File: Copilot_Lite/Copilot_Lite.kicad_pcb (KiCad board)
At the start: 4 copper layers, 65 x 56 mm, 80 parts, among them J1 POWER_MODES, J11 SERIAL_MODE, J12 SERIAL_VOLTAGE_SELECT, J2 JACK_POWER_IN, J3 USB_POWER_IN, J4 USB_PC, J6 5V_ENABLE, J7 SERIAL_AND_GPIO, J8 JACK_POWER_OUT, J9 USB_POWER_OUT, Q1 BSS138, Q2 BUK7M27-80EX, Q3 BUK7M27-80EX, Q4 BSS138, Q5 BSS138, Q6 BSS138, Q7 BSS138, Q8 BSS138, Q9 BSS138, U1 LM74502, U2 LM74502, U3 AP2204K-ADJ, U4 AP2204K-ADJ, U5 FT230XS, U6 SN74LV1T125, U7 SN74LV1T125, U8 SN74LV1T125, U9 SN74LV1T125

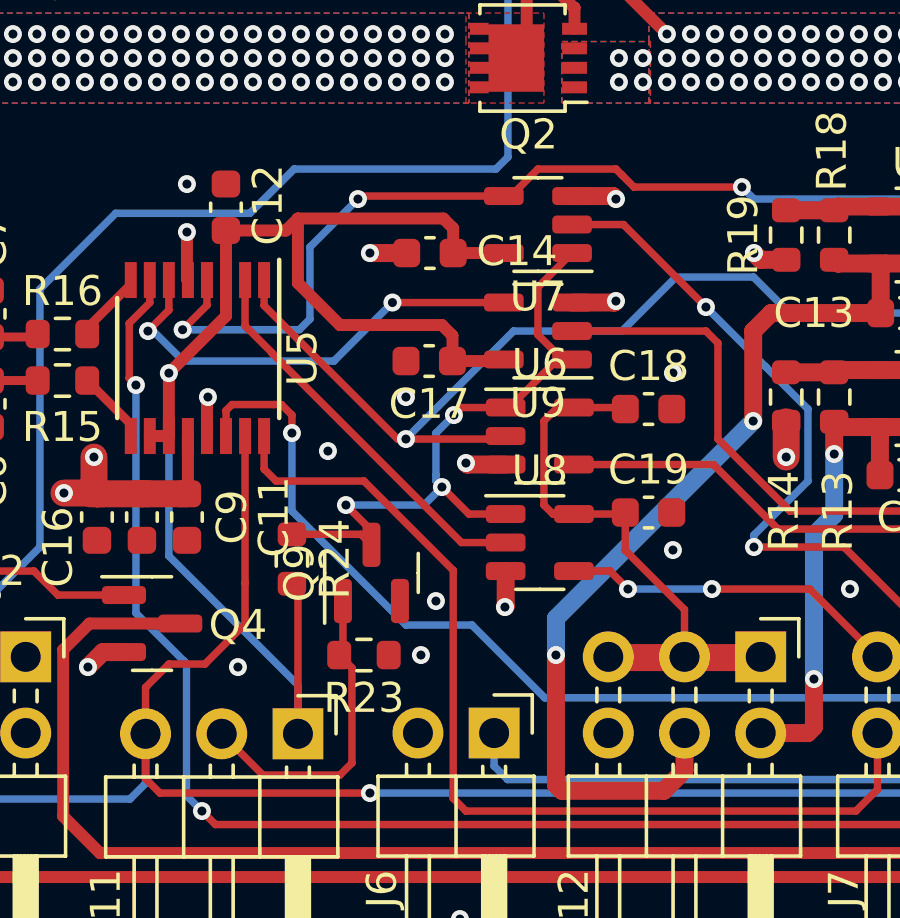
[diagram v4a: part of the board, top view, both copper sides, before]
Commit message: lite: Cleaned PCB silkscreen and fixed all warnings.
Signed-off-by: Adrien Ricciardi <aricciardi@baylibre.com>
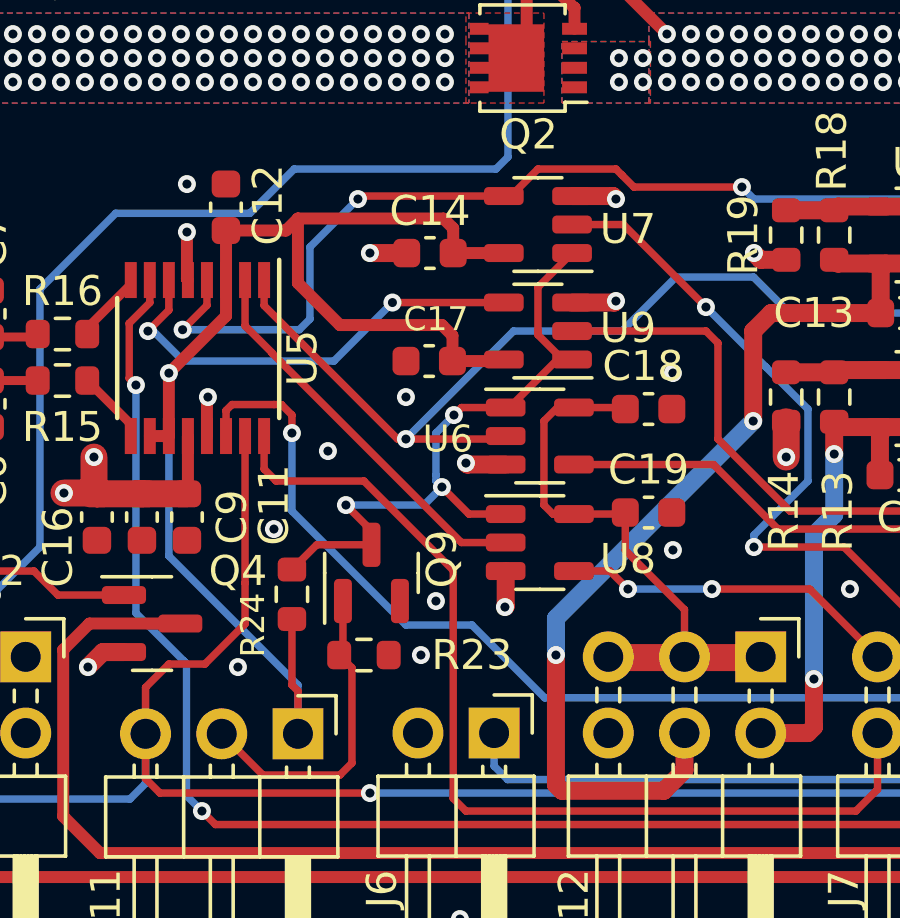
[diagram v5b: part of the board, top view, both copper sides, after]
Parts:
- moved R24 1.17 mm to (89.4, 101.4)
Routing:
- net +3.3VA: track 48.2 -> 47.0 mm
- net GND: vias 59 -> 60
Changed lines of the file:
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@@
     (property "Sheetname" "Controller")
     (attr smd)
-    (fp_text reference "U9" (at 0 -2.4) (layer "F.SilkS")
+    (fp_text reference "U9" (at -3 0.1) (layer "F.SilkS")
         (effects (font (size 1 1) (thickness 0.15)))
     )
@@
     (property "Sheetname" "Controller")
     (attr smd)
-    (fp_text reference "U7" (at 0 -2.4) (layer "F.SilkS")
+    (fp_text reference "U7" (at -3 -0.15) (layer "F.SilkS")
         (effects (font (size 1 1) (thickness 0.15)))
     )
@@
     (property "Sheetname" "Controller")
     (attr smd)
-    (fp_text reference "U6" (at 0 -2.4) (layer "F.SilkS")
-        (effects (font (size 1 1) (thickness 0.15)))
+    (fp_text reference "U6" (at -3.0625 0.1) (layer "F.SilkS")
+        (effects (font (size 0.9 0.9) (thickness 0.15)))
     )
     (fp_text value "SN74LV1T125" (at 0 2.4) (layer "F.Fab") hide
@@
     (property "ki_keywords" "cap capacitor")
     (attr smd)
-    (fp_text reference "C18" (at 0 -1.43) (layer "F.SilkS")
+    (fp_text reference "C18" (at -0.1875 -1.43) (layer "F.SilkS")
         (effects (font (size 1 1) (thickness 0.15)))
     )
@@
     (property "ki_keywords" "cap capacitor")
     (attr smd)
-    (fp_text reference "C14" (at -2.9 0.06) (layer "F.SilkS")
+    (fp_text reference "C14" (at 0 1.4) (layer "F.SilkS")
         (effects (font (size 1 1) (thickness 0.15)))
     )
@@
     (property "ki_keywords" "R res resistor")
     (attr smd)
-    (fp_text reference "R23" (at 0 -1.43) (layer "F.SilkS")
+    (fp_text reference "R23" (at -3.6 0) (layer "F.SilkS")
         (effects (font (size 1 1) (thickness 0.15)))
     )
@@
     (property "ki_keywords" "N-Channel MOSFET")
     (attr smd)
-    (fp_text reference "Q4" (at 2.8625 0.05) (layer "F.SilkS")
+    (fp_text reference "Q4" (at 2.8625 -1.75) (layer "F.SilkS")
         (effects (font (size 1 1) (thickness 0.15)))
     )
@@
     (property "ki_keywords" "N-Channel MOSFET")
     (attr smd)
-    (fp_text reference "Q9" (at 0 -2.4 90) (layer "F.SilkS")
+    (fp_text reference "Q9" (at 0.4625 2.35 90) (layer "F.SilkS")
         (effects (font (size 1 1) (thickness 0.15)))
     )
@@
     (property "Sheetname" "Controller")
     (attr smd)
-    (fp_text reference "U8" (at 0 -2.4) (layer "F.SilkS")
+    (fp_text reference "U8" (at 2.9375 0.55) (layer "F.SilkS")
         (effects (font (size 1 1) (thickness 0.15)))
     )
@@
   )
   (footprint "Resistor_SMD:R_0603_1608Metric" (layer "F.Cu")
-    (at 89.4 100.2 -90)
+    (at 89.4 101.375 -90)
     (descr "Resistor SMD 0603 (1608 Metric), square (rectangular) end terminal, IPC_7351 nominal, (Body size source: IPC-SM-782 page 72, https://www.pcb-3d.com/wordpress/wp-content/uploads/ipc-sm-782a_amendment_1_and_2.pdf), generated with kicad-footprint-generator")
     (tags "resistor")
@@
     (property "ki_keywords" "R res resistor")
     (attr smd)
-    (fp_text reference "R24" (at 0 -1.43 90) (layer "F.SilkS")
-        (effects (font (size 1 1) (thickness 0.15)))
+    (fp_text reference "R24" (at 1.025 1.3 90) (layer "F.SilkS")
+        (effects (font (size 0.8 0.8) (thickness 0.15)))
     )
     (fp_text value "10K" (at 0 1.43 90) (layer "F.Fab") hide
@@
     (property "ki_keywords" "cap capacitor")
     (attr smd)
-    (fp_text reference "C11" (at 0 -2.9 90) (layer "F.SilkS")
+    (fp_text reference "C11" (at -0.4 -2.9 90) (layer "F.SilkS")
         (effects (font (size 1 1) (thickness 0.15)))
     )
@@
     (property "ki_keywords" "cap capacitor")
     (attr smd)
-    (fp_text reference "C17" (at 0 -1.43) (layer "F.SilkS")
-        (effects (font (size 1 1) (thickness 0.15)))
+    (fp_text reference "C17" (at -0.225 1.4) (layer "F.SilkS")
+        (effects (font (size 0.8 0.8) (thickness 0.15)))
     )
     (fp_text value "100n" (at 0 1.43) (layer "F.Fab") hide
@@
   (via (at 105.875 96.8) (size 0.6) (drill 0.3) (layers "F.Cu" "B.Cu") (free) (net 2))
   (via (at 92 90) (size 0.6) (drill 0.3) (layers "F.Cu" "B.Cu") (free) (net 2))
+  (via (at 88.8 99.2) (size 0.6) (drill 0.3) (layers "F.Cu" "B.Cu") (free) (net 2))
   (via (at 70.2 72.8) (size 0.6) (drill 0.3) (layers "F.Cu" "B.Cu") (free) (net 2))
   (via (at 65.5 77.5) (size 0.6) (drill 0.3) (layers "F.Cu" "B.Cu") (free) (net 2))
@@
   (segment (start 87.2025 90.9) (end 87.2025 92.0975) (width 0.4) (layer "F.Cu") (net 9))
   (segment (start 94.775 89.175) (end 94.45 88.85) (width 0.4) (layer "F.Cu") (net 9))
-  (segment (start 89.6 101.225) (end 89.6 106.025) (width 0.25) (layer "F.Cu") (net 9))
   (segment (start 85.2975 94.0025) (end 85.2975 96.1) (width 0.4) (layer "F.Cu") (net 9))
   (segment (start 94.75 92.75) (end 94.4 92.4) (width 0.4) (layer "F.Cu") (net 9))
+  (segment (start 89.4 102.2) (end 89.4 104.4) (width 0.25) (layer "F.Cu") (net 9))
   (segment (start 94.75 93.6) (end 96.4125 93.6) (width 0.4) (layer "F.Cu") (net 9))
   (segment (start 87.2 89.25) (end 89.2 89.25) (width 0.4) (layer "F.Cu") (net 9))
+  (segment (start 89.4 104.4) (end 89.6 104.6) (width 0.25) (layer "F.Cu") (net 9))
   (segment (start 94.775 90) (end 96.4625 90) (width 0.4) (layer "F.Cu") (net 9))
   (segment (start 89.2 89.25) (end 89.6 88.85) (width 0.4) (layer "F.Cu") (net 9))
@@
   (segment (start 94.75 93.6) (end 94.75 92.75) (width 0.4) (layer "F.Cu") (net 9))
   (segment (start 94.4 92.4) (end 91 92.4) (width 0.4) (layer "F.Cu") (net 9))
-  (segment (start 89.4 101.025) (end 89.6 101.225) (width 0.25) (layer "F.Cu") (net 9))
   (segment (start 94.45 88.85) (end 89.6 88.85) (width 0.4) (layer "F.Cu") (net 9))
   (segment (start 87.2025 89.2525) (end 87.2 89.25) (width 0.4) (layer "F.Cu") (net 9))
@@
   (segment (start 94.775 90) (end 94.775 89.175) (width 0.4) (layer "F.Cu") (net 9))
   (segment (start 87.2025 90.9) (end 87.2025 89.2525) (width 0.4) (layer "F.Cu") (net 9))
+  (segment (start 89.6 104.6) (end 89.6 106.025) (width 0.25) (layer "F.Cu") (net 9))
   (segment (start 89.6 91) (end 91 92.4) (width 0.4) (layer "F.Cu") (net 9))
   (segment (start 87.2025 92.0975) (end 85.2975 94.0025) (width 0.4) (layer "F.Cu") (net 9))
@@
   (segment (start 102.485 101.885) (end 102.485 103.46) (width 0.25) (layer "F.Cu") (net 78))
   (segment (start 97.8 95.6) (end 97.8 98.4) (width 0.25) (layer "F.Cu") (net 78))
-  (segment (start 89.4 99.375) (end 91.7 99.375) (width 0.25) (layer "F.Cu") (net 79))
   (segment (start 96.525 95.15) (end 95.05 95.15) (width 0.25) (layer "F.Cu") (net 79))
   (segment (start 98.7375 93.55) (end 98.423959 93.55) (width 0.25) (layer "F.Cu") (net 79))
+  (segment (start 90.225 99.725) (end 89.4 100.55) (width 0.25) (layer "F.Cu") (net 79))
   (segment (start 98.25 93.55) (end 98.7375 93.55) (width 0.25) (layer "F.Cu") (net 79))
   (segment (start 96.65 95.15) (end 98.25 93.55) (width 0.25) (layer "F.Cu") (net 79))
@@
   (segment (start 98.7375 90) (end 97.6 91.1375) (width 0.25) (layer "F.Cu") (net 79))
   (segment (start 92.05 99.725) (end 92.05 99.25) (width 0.25) (layer "F.Cu") (net 79))
-  (segment (start 91.7 99.375) (end 92.05 99.725) (width 0.25) (layer "F.Cu") (net 79))
   (segment (start 96.525 98.7) (end 95.3 98.7) (width 0.25) (layer "F.Cu") (net 79))
   (segment (start 95.05 95.15) (end 94.8 95.4) (width 0.25) (layer "F.Cu") (net 79))
   (segment (start 95.3 98.7) (end 94.4 97.8) (width 0.25) (layer "F.Cu") (net 79))
+  (segment (start 92.05 99.725) (end 90.225 99.725) (width 0.25) (layer "F.Cu") (net 79))
   (segment (start 97.6 91.1375) (end 97.6 92.6) (width 0.25) (layer "F.Cu") (net 79))
   (via (at 94.8 95.4) (size 0.6) (drill 0.3) (layers "F.Cu" "B.Cu") (net 79))
